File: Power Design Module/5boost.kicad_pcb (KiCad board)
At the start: 2 copper layers, 15 parts, among them J1 105430-1102, J2 105430-1102, J3 105430-1102, U1 TPS61232DRCR, U2 TPPM0110DWPR

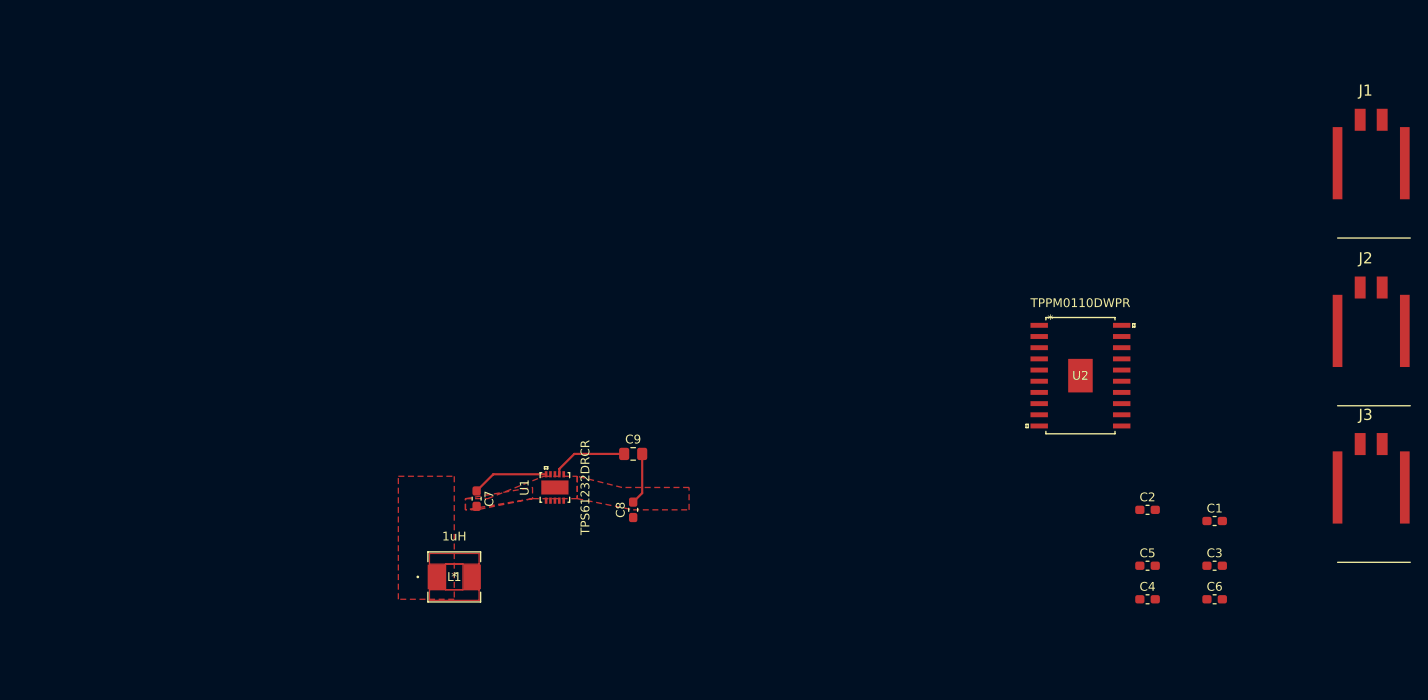
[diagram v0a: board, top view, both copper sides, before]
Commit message: Charging circuit and rough layout
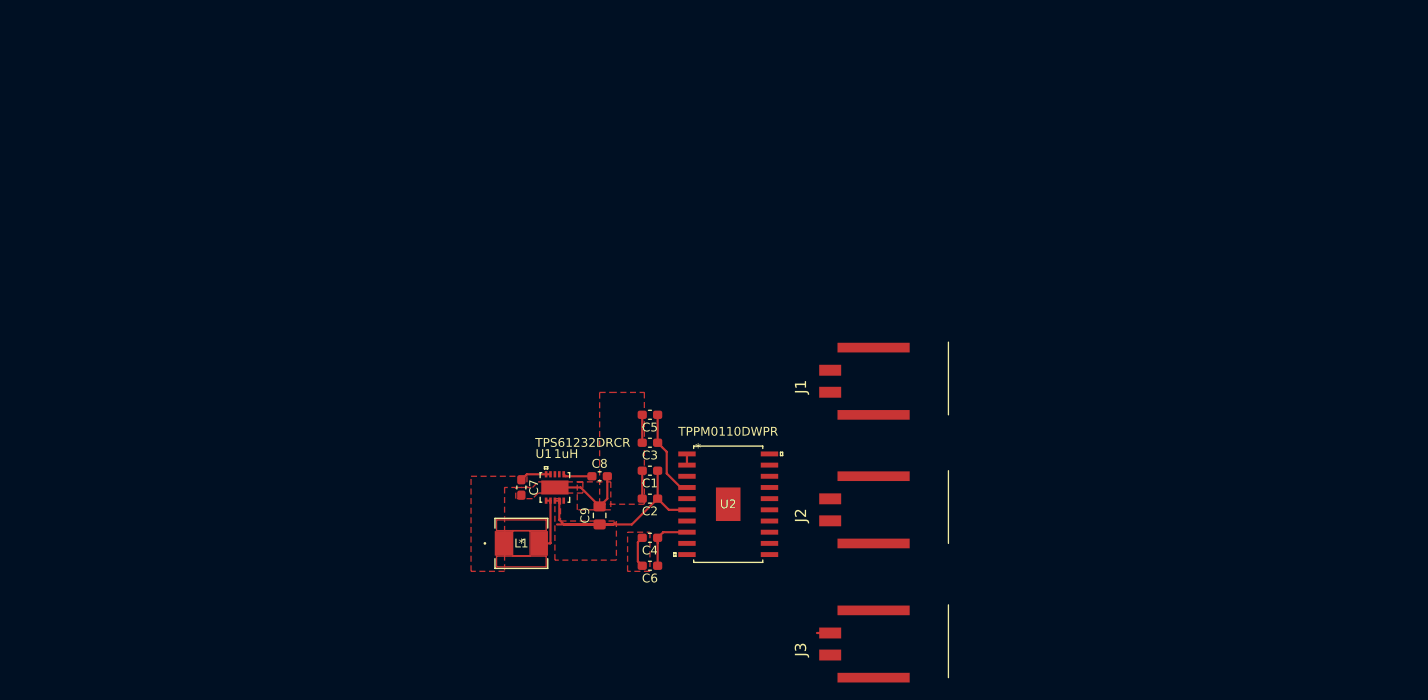
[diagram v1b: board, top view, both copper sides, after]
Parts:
- moved C3 65.6 mm to (141.6, 85.1), turned to 180 degrees
- moved C1 64.4 mm to (141.6, 88.3), turned to 180 degrees
- moved C6 64.2 mm to (141.6, 99.1), turned to 180 degrees
- moved J1 61.7 mm to (167.0, 78.1), turned to 90 degrees
- moved J2 60.1 mm to (167.0, 92.7), turned to 90 degrees
- moved J3 59.2 mm to (167.0, 108.0), turned to 90 degrees
- moved C5 59.1 mm to (141.6, 81.9), turned to 180 degrees
- moved C4 56.9 mm to (141.6, 95.9), turned to 180 degrees
- moved C2 56.5 mm to (141.6, 91.4), turned to 180 degrees
- moved U2 42.6 mm to (150.5, 92.1)
- moved L1 8.52 mm to (127.0, 96.5)
- moved C9 7.96 mm to (135.9, 93.3), turned to 90 degrees
- moved C8 5.39 mm to (135.9, 88.9), turned to 0 degrees
- moved C7 5.24 mm to (127.0, 90.2)
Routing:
- net Net-(C1-Pad1): track 8.68 -> 31.4 mm
- net GND: track 5.90 -> 20.3 mm
- net Net-(C3-Pad1): track 0.00 -> 10.1 mm
- net Net-(C4-Pad1): track 0.00 -> 8.85 mm
- net Net-(L1-Pad2): track 0.00 -> 6.61 mm
- net /ChargingCircuit/Voutbat: track 8.67 -> 3.57 mm
- net Net-(C8-Pad1): track 0.00 -> 3.30 mm
- net (no net): track 0.00 -> 1.27 mm
- added copper zone on F.Cu, net Net-(C1-Pad1)

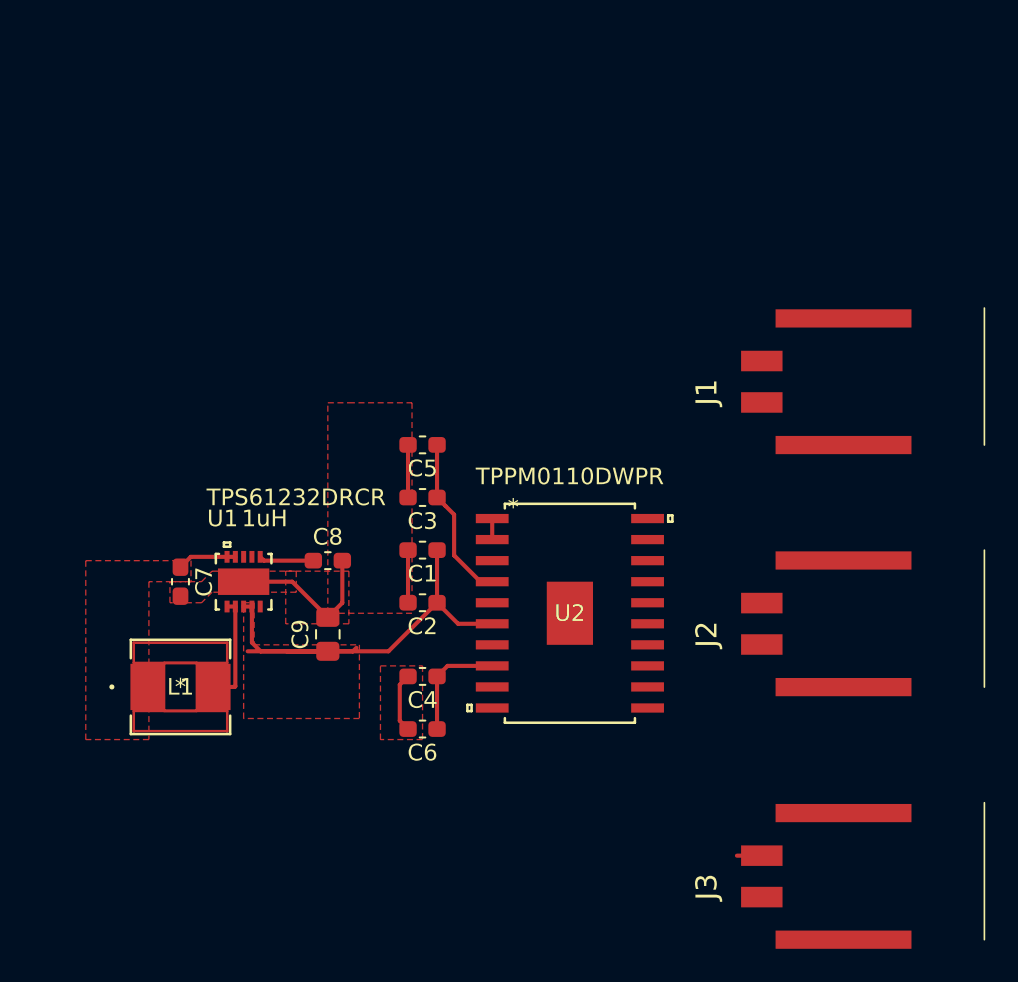
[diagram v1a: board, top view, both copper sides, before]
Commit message: Starting Power board Layout. Design Changes
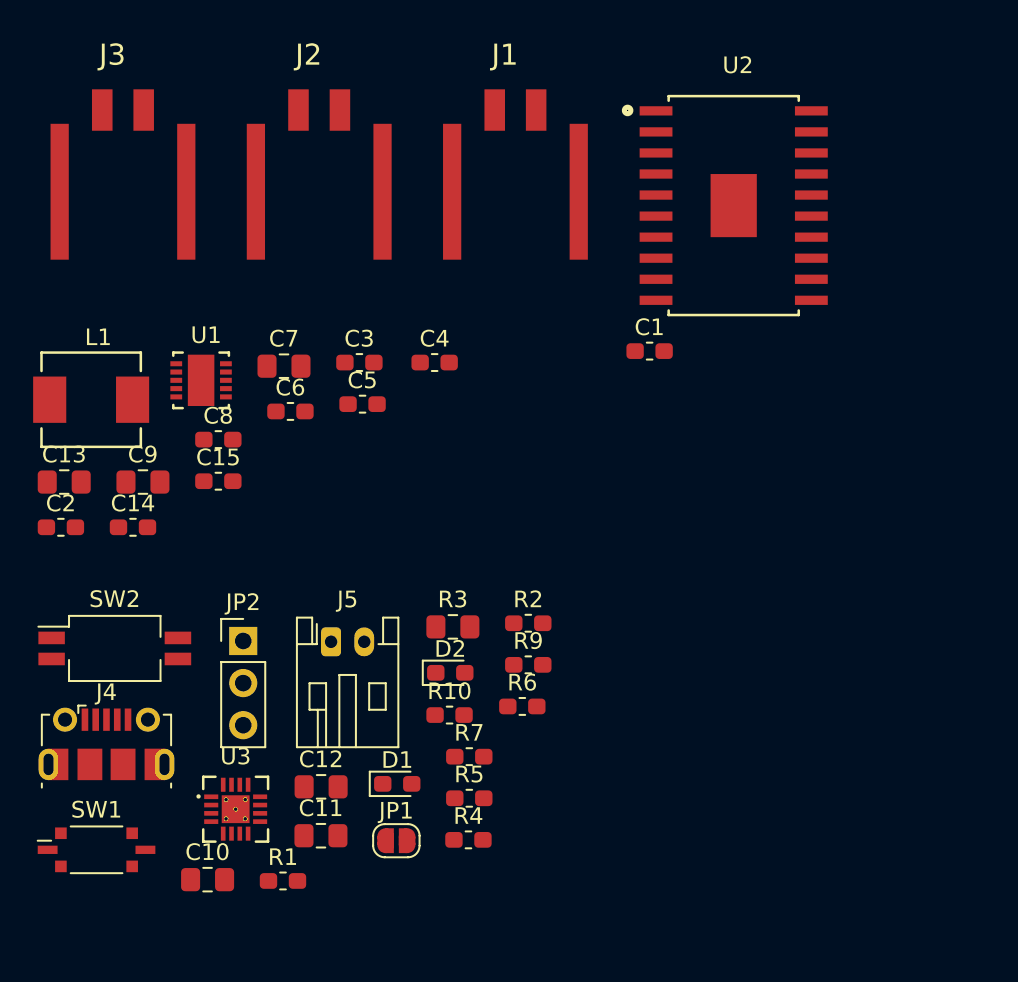
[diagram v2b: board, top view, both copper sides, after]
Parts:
- added C10: 1uF, Capacitor_SMD:C_0805_2012Metric_Pad1.15x1.40mm_HandSolder, F.Cu at (128.6, 108.1)
- added C11: 4.7uF, Capacitor_SMD:C_0805_2012Metric_Pad1.15x1.40mm_HandSolder, F.Cu at (135.5, 105.5)
- added C12: 4.7uF, Capacitor_SMD:C_0805_2012Metric_Pad1.15x1.40mm_HandSolder, F.Cu at (135.5, 102.5)
- added C13: 10uF, Capacitor_SMD:C_0805_2012Metric_Pad1.15x1.40mm_HandSolder, F.Cu at (120.0, 84.2)
- added C14: 0.1uF, Capacitor_SMD:C_0603_1608Metric_Pad1.05x0.95mm_HandSolder, F.Cu at (124.1, 86.9)
- added C15: 10uF, Capacitor_SMD:C_0603_1608Metric_Pad1.05x0.95mm_HandSolder, F.Cu at (129.3, 84.1)
- added D1: Red, LED_SMD:LED_0603_1608Metric_Pad1.05x0.95mm_HandSolder, F.Cu at (140.1, 102.4)
- added D2: Green, LED_SMD:LED_0603_1608Metric_Pad1.05x0.95mm_HandSolder, F.Cu at (143.3, 95.7)
- added J4: USB_B_Micro, Connector_USB:USB_Micro-B_Molex-105017-0001, F.Cu at (122.5, 100.0)
- added J5: Battery Output, Connector_JST:JST_PH_S2B-PH-K_1x02_P2.00mm_Horizontal, F.Cu at (136.1, 93.8)
- added JP1: TMR OFF, Jumper:SolderJumper-2_P1.3mm_Open_RoundedPad1.0x1.5mm, F.Cu at (140.0, 105.8)
- added JP2: Charger / Battery Bypass, Connector_PinHeader_2.54mm:PinHeader_1x03_P2.54mm_Vertical, F.Cu at (130.8, 93.7)
- added R1: 2K, Resistor_SMD:R_0603_1608Metric_Pad1.05x0.95mm_HandSolder, F.Cu at (133.2, 108.2)
- added R10: 10k, Resistor_SMD:R_0603_1608Metric_Pad1.05x0.95mm_HandSolder, F.Cu at (143.2, 98.2)
- added R2: 2K, Resistor_SMD:R_0603_1608Metric_Pad1.05x0.95mm_HandSolder, F.Cu at (148.0, 92.7)
- added R3: 1.78k, Resistor_SMD:R_0805_2012Metric_Pad1.15x1.40mm_HandSolder, F.Cu at (143.4, 92.9)
- added R4: 530R, Resistor_SMD:R_0603_1608Metric_Pad1.05x0.95mm_HandSolder, F.Cu at (144.4, 105.7)
- added R5: 320R, Resistor_SMD:R_0603_1608Metric_Pad1.05x0.95mm_HandSolder, F.Cu at (144.4, 103.2)
- added R6: 200k, Resistor_SMD:R_0603_1608Metric_Pad1.05x0.95mm_HandSolder, F.Cu at (147.6, 97.7)
- added R7: 49.9k, Resistor_SMD:R_0603_1608Metric_Pad1.05x0.95mm_HandSolder, F.Cu at (144.4, 100.7)
- added R9: 10k, Resistor_SMD:R_0603_1608Metric_Pad1.05x0.95mm_HandSolder, F.Cu at (148.0, 95.2)
- added SW1: Charge Disable Switch, Button_Switch_SMD:SW_DIP_SPSTx01_Slide_Copal_CVS-01xB_W5.9mm_P1mm, F.Cu at (121.9, 106.3)
- added SW2: Input Current Selection, Button_Switch_SMD:SW_DIP_SPSTx02_Slide_Copal_CHS-02B_W7.62mm_P1.27mm, F.Cu at (123.0, 94.2)
- added U3: BQ24072TRGTR, BQ24072TRGTR:BQ24072TRGTR, F.Cu at (130.3, 103.9)
- C1, C5: value 10uF -> 10μF
- C3: value 0.1uF -> 10μF
- C7: value 10μF -> 10uF; footprint Capacitor_SMD:C_0603_1608Metric_Pad1.05x0.95mm_HandSolder -> Capacitor_SMD:C_0805_2012Metric_Pad1.15x1.40mm_HandSolder
- C8: value 15nF -> 22nF
- moved J3 60.0 mm to (123.5, 66.6), turned to 0 degrees
- moved J2 41.0 mm to (135.4, 66.6), turned to 0 degrees
- moved U2 26.5 mm to (160.4, 67.5)
- moved J1 22.9 mm to (147.2, 66.6), turned to 0 degrees
- moved C2 22.3 mm to (119.8, 86.9), turned to 0 degrees
- moved C6 20.8 mm to (133.6, 79.9), turned to 0 degrees
- moved C4 19.0 mm to (142.3, 76.9), turned to 0 degrees
- moved C1 18.2 mm to (155.3, 76.3), turned to 0 degrees
- moved L1 18.2 mm to (121.6, 79.2)
- moved C9 14.5 mm to (124.7, 84.2), turned to 0 degrees
- moved C7 14.4 mm to (133.2, 77.2), turned to 0 degrees
- moved U1 12.4 mm to (128.2, 78.0), turned to 0 degrees
- moved C8 9.85 mm to (129.3, 81.6)
- moved C3 8.99 mm to (137.8, 76.9), turned to 0 degrees
- moved C5 4.38 mm to (138.0, 79.5), turned to 0 degrees
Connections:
- C1 pad 1: Net-(C1-Pad1) -> GND
- C1 pad 2: GND -> /Voutbat
- C2 pad 1: Net-(C1-Pad1) -> /5.0V
- C3 pad 1: Net-(C3-Pad1) -> GND
- C3 pad 2: GND -> /Voutbat
- C4 pad 1: Net-(C4-Pad1) -> /1.8V
- C5 pad 1: Net-(C3-Pad1) -> GND
- C5 pad 2: GND -> /Voutbat
- C6 pad 1: Net-(C4-Pad1) -> /1.8V
- C7 pad 1: /ChargingCircuit/Voutbat -> /5.0V
- C9 pad 1: Net-(C1-Pad1) -> /5.0V
- J1 pad 1: Net-(C1-Pad1) -> GND
- J1 pad 2: (no net) -> /5.0V
- J1 pad 4: GND -> /5.0V
- J2 pad 1: Net-(C3-Pad1) -> GND
- J2 pad 2: (no net) -> /3.3V
- J2 pad 4: GND -> /3.3V
- J3 pad 1: Net-(C4-Pad1) -> GND
- J3 pad 2: (no net) -> /1.8V
- J3 pad 4: GND -> /1.8V
- L1 pad 1: /ChargingCircuit/Voutbat -> /Voutbat
- U1 pad 10: /ChargingCircuit/Voutbat -> /Voutbat
- U1 pad 3: Net-(C1-Pad1) -> /5.0V
- U1 pad 4: Net-(C1-Pad1) -> /5.0V
- U1 pad 5: (no net) -> Net-(U1-Pad5)
- U1 pad 7: Net-(C1-Pad1) -> /5.0V
- U1 pad 8: (no net) -> Net-(U1-Pad8)
- U1 pad 9: /ChargingCircuit/Voutbat -> /Voutbat
- U2 pad 4: Net-(C3-Pad1) -> /3.3V
- U2 pad 6: Net-(C1-Pad1) -> /5.0V
- U2 pad 8: Net-(C4-Pad1) -> /1.8V
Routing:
- net Net-(C1-Pad1): track 31.4 -> 0.00 mm
- net GND: track 20.3 -> 0.00 mm
- net Net-(C3-Pad1): track 10.1 -> 0.00 mm
- net Net-(C4-Pad1): track 8.85 -> 0.00 mm
- net Net-(L1-Pad2): track 6.61 -> 0.00 mm
- net /ChargingCircuit/Voutbat: track 3.57 -> 0.00 mm
- net Net-(C8-Pad1): track 3.30 -> 0.00 mm
- net (no net): track 1.27 -> 0.00 mm
- removed copper zone on F.Cu, net /ChargingCircuit/Voutbat
- removed copper zone on F.Cu, net GND
- removed copper zone on F.Cu, net Net-(C1-Pad1)

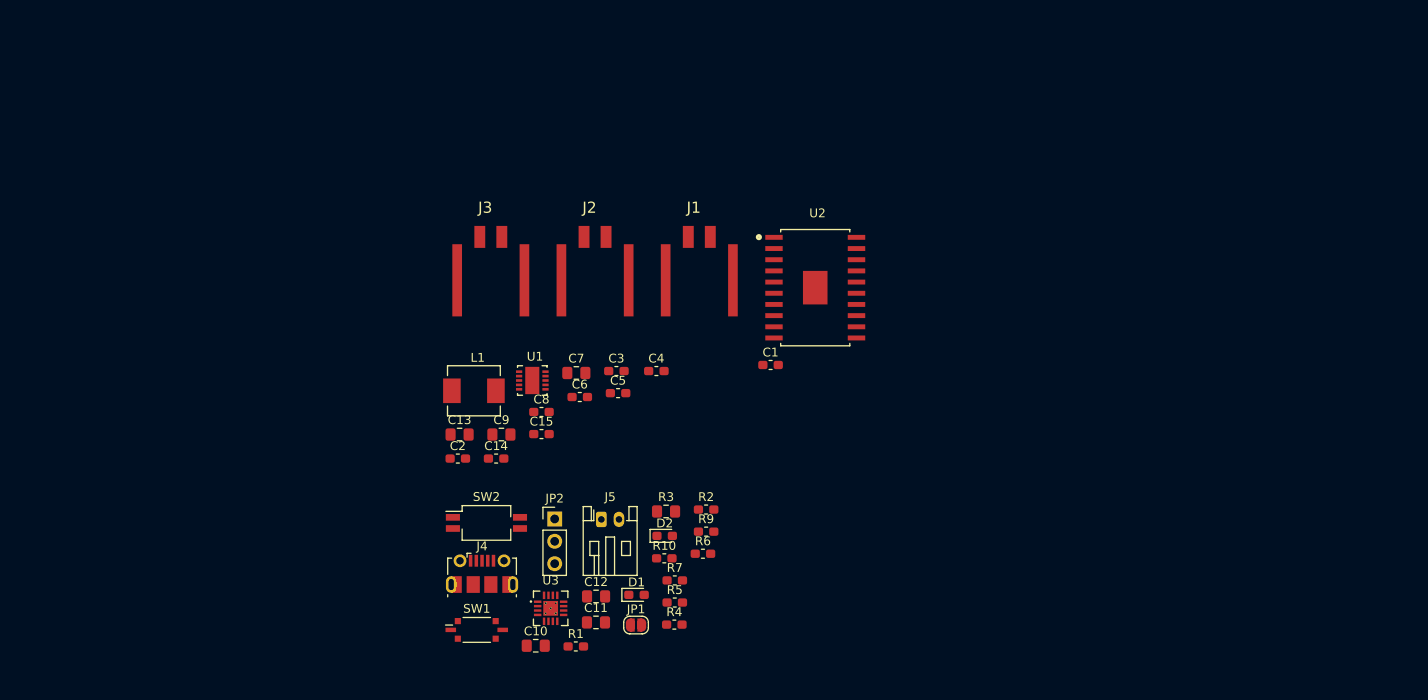
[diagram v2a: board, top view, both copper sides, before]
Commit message: Final Power Breakout completed. Headers were used instead of the previous Molex Connectors
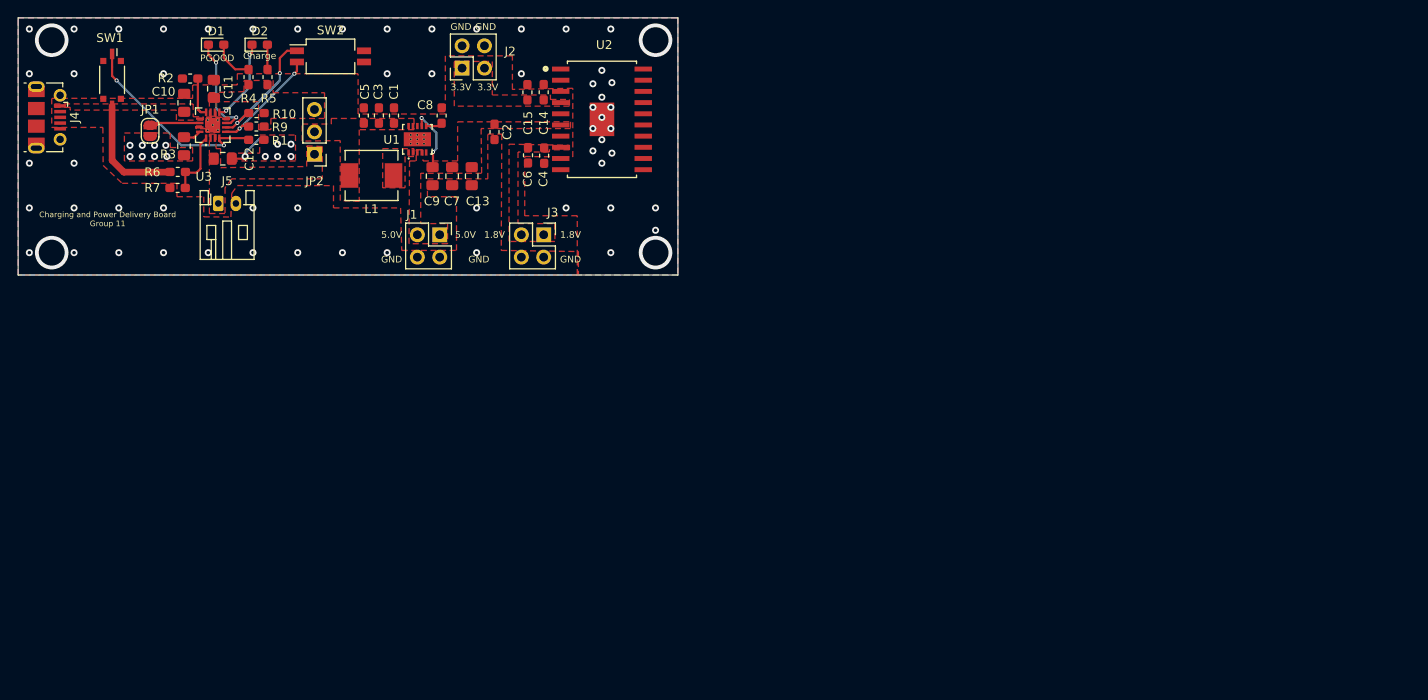
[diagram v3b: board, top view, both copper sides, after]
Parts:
- J1: value 105430-1102 -> 5.0V; footprint 105430-1102:1054301102 -> Connector_PinSocket_2.54mm:PinSocket_2x02_P2.54mm_Vertical
- J2: value 105430-1102 -> 3.3V; footprint 105430-1102:1054301102 -> Connector_PinSocket_2.54mm:PinSocket_2x02_P2.54mm_Vertical
- J3: value 105430-1102 -> 1.8V; footprint 105430-1102:1054301102 -> Connector_PinSocket_2.54mm:PinSocket_2x02_P2.54mm_Vertical
- U1: value TPS61232DRCR -> DRC_S-PVSON-N10
- moved R4 78.8 mm to (96.0, 43.6), turned to 90 degrees
- moved JP1 78.7 mm to (84.8, 49.7), turned to 270 degrees
- moved D1 78.6 mm to (92.3, 39.9)
- moved R2 76.4 mm to (89.4, 43.7), turned to 180 degrees
- moved R5 75.5 mm to (98.2, 43.6), turned to 90 degrees
- moved SW1 75.0 mm to (80.5, 43.9), turned to 270 degrees
- moved C11 74.5 mm to (92.1, 44.9), turned to 90 degrees
- moved R6 73.7 mm to (88.0, 54.3)
- moved C10 73.5 mm to (88.7, 46.5), turned to 90 degrees
- moved D2 72.3 mm to (97.3, 39.9)
- moved R7 71.9 mm to (88.0, 56.1), turned to 180 degrees
- moved J4 71.6 mm to (73.2, 48.1), turned to 270 degrees
- moved R9 68.8 mm to (96.9, 49.2)
- moved R3 68.7 mm to (88.7, 51.4), turned to 270 degrees
- moved R10 68.6 mm to (96.9, 47.7), turned to 180 degrees
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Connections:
- J1 pad 1: GND -> /5.0V
- J1 pad 4: /5.0V -> GND
- J2 pad 1: GND -> /3.3V
- J2 pad 4: /3.3V -> GND
- J3 pad 1: GND -> /1.8V
- J3 pad 4: /1.8V -> GND
- R10 pad 2: EN2 -> EN1
- R9 pad 1: EN1 -> EN2
- SW2 pad 1: EN2 -> EN1
- SW2 pad 2: EN1 -> EN2
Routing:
- net ~CE: track 0.00 -> 22.8 mm, vias 0 -> 2
- net EN1: track 0.00 -> 21.6 mm, vias 0 -> 2
- net EN2: track 0.00 -> 13.2 mm, vias 0 -> 2
- net Vbus: track 0.00 -> 13.1 mm
- net Net-(D1-Pad1): track 0.00 -> 11.8 mm, vias 0 -> 2
- net Net-(D2-Pad1): track 0.00 -> 9.56 mm, vias 0 -> 2
- net /5.0V: track 0.00 -> 7.41 mm, vias 0 -> 2
- net Net-(R6-Pad2): track 0.00 -> 7.33 mm
- net Net-(JP1-Pad1): track 0.00 -> 6.47 mm
- net Net-(R2-Pad1): track 0.00 -> 4.92 mm
- net Net-(D1-Pad2): track 0.00 -> 4.85 mm
- net GND: track 0.00 -> 4.52 mm, vias 0 -> 73
- net Net-(D2-Pad2): track 0.00 -> 2.80 mm
- net Net-(R3-Pad1): track 0.00 -> 2.09 mm
- net Net-(C8-Pad1): track 0.00 -> 1.94 mm
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- added copper zone on F.Cu, net /1.8V
- added copper zone on F.Cu, net /3.3V
- added copper zone on F.Cu, net /5.0V
- added copper zone on F.Cu, net /ChargingCircuit/BATT+
- added copper zone on F.Cu, net /Voutbat
- added copper zone on B.Cu, net GND
- added copper zone on F.Cu, net GND
- added copper zone on F.Cu, net Net-(L1-Pad2)
- added copper zone on F.Cu, net Vbus
- added copper zone on F.Cu, net Vout
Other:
- board outline added: 74.9 x 29.2 mm
- net class Default: clearance 0.2 -> 0.0889; via_dia 0.8 -> 0.4572; via_drill 0.4 -> 0.254
- rule trace_clearance: 0.2 -> 0.0889
- rule trace_min: 0.2 -> 0.1016
- rule via_min_drill: 0.3 -> 0.199898
- rule via_min_size: 0.4 -> 0.45
- board text added: "1.8V"
- board text added: "3.3V"
- board text added: "5.0V"
- board text added: "Charge"
- board text added: "Charging and Power Delivery Board Group 11"
- board text added: "GND"
- board text added: "PGOOD"
